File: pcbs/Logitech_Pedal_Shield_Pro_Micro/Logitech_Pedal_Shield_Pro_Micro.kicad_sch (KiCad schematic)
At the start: 11 parts, among them J1 DB9_Female_MountingHoles, J2 AVR-ISP-6, U1 SparkFun_ProMicro

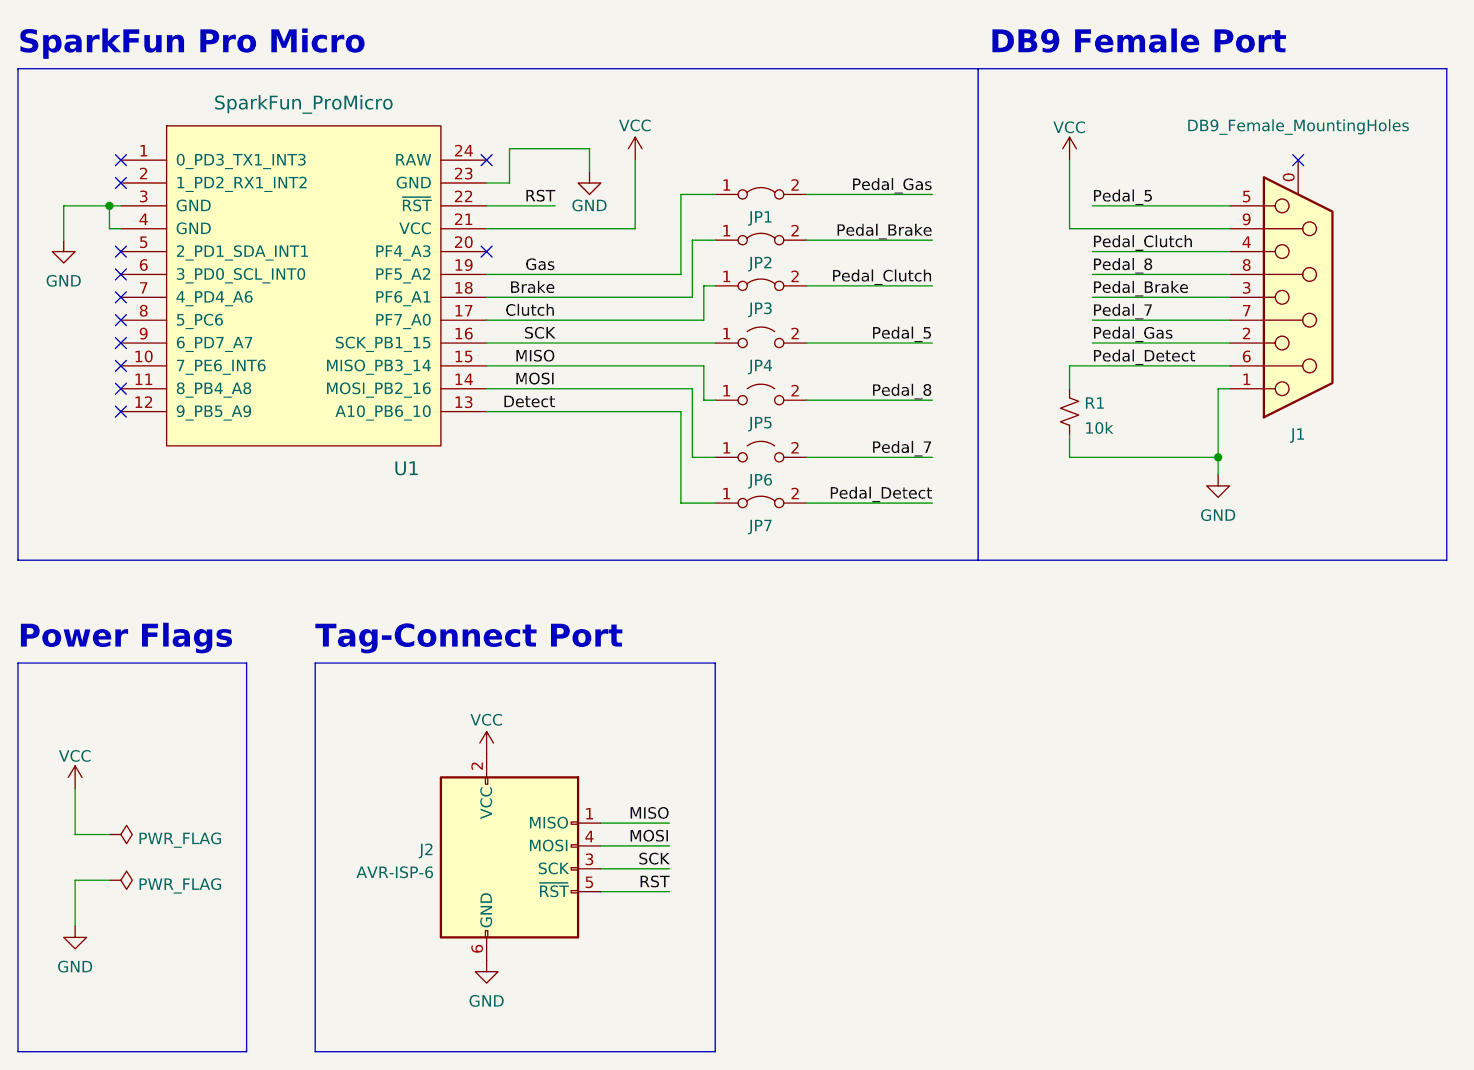
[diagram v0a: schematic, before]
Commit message: KiCad 8 Format Updates (#4)
* Add KiCad files to gitignore
* Update PCBs to KiCad8 format (8.0.8)
* Relink DE-9 connector symbols
* Update modified schematic symbols
* Pedals: Fix 'wire off grid' schematic error
* Set min_copper_edge_clearance
* Update PCBs from schematic

This updates the format of the PCB files to be compatible with KiCad 8 There are no intended functional changes.
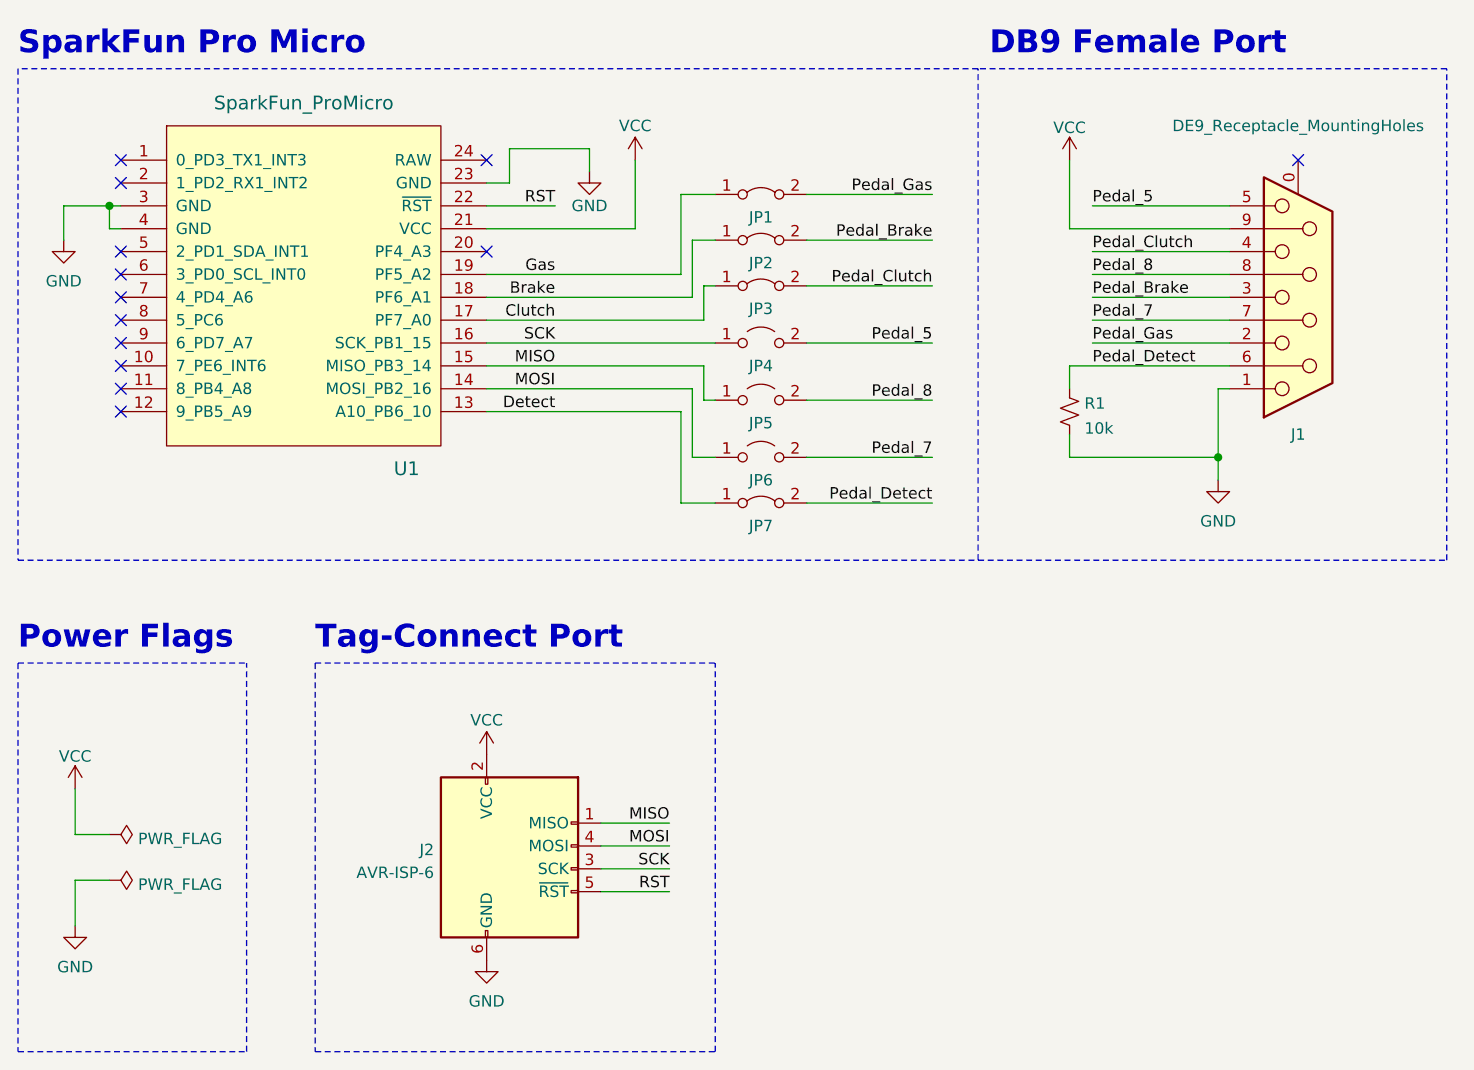
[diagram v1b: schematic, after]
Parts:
- J1: value DB9_Female_MountingHoles -> DE9_Receptacle_MountingHoles; symbol Connector:DB9_Female_MountingHoles -> Connector:DE9_Receptacle_MountingHoles
- JP1, JP2, JP3, JP7: footprint (none) -> Sim_Racing_Shields:SolderJumper-2_P1.3mm_Bridged_RoundedPad1.0x1.5mm_Unmasked
- U1: footprint (none) -> Sim_Racing_Shields:Sparkfun_ProMicro

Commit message: Bill of Materials (BOM) (#5)
Adds Bill of Materials (BOM) information to the KiCad schematic, which can be exported to CSV using the "Generate Bill of Materials" option in the toolbar of the schematic editor.

These parts are, to the best of my knowledge, the parts I used when assembling these boards two and a half years ago. You do not need to use these exact parts, substitutes may be available that are currently stocked and/or less expensive. The 1% resistors, in particular, do not need to be tight tolerance - that's just what I had on hand.
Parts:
- J1: DigiKey Part Number (none) -> AE10921-ND; Manufacturer (none) -> Assmann WSW Components; Part Number (none) -> A-DF 09 A/KG-T2S
- J2, JP4, JP5, JP6: now left out of the parts list
- R1: DigiKey Part Number (none) -> YAG1319CT-ND; Manufacturer (none) -> YAGEO; Part Number (none) -> RC0805FR-0710KP
- U1: DigiKey Part Number (none) -> 1568-DEV-15795-ND; Manufacturer (none) -> SparkFun Electronics; Part Number (none) -> DEV-15795
